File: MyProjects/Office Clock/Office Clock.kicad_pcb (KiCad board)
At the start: 2 copper layers, 105.4 x 97.8 mm, 13 parts, among them M1 DLX3416, M2 DLX3416, Q1 Q_Photo_NPN_CE, U1 MAX7219, U2 D1_Mini, U3 74HCT367N, U4 74HCT164N

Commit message: Finished schematic wiring
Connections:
- M1 pad 1: Net-(M1-Pad1) -> +5V
- M1 pad 10: Net-(M1-Pad10) -> +5V
- M1 pad 11: Net-(M1-Pad11) -> GND
- M1 pad 12: Net-(M1-Pad12) -> GND
- M1 pad 14: Net-(M1-Pad14) -> +5V
- M1 pad 16: Net-(M1-Pad16) -> /d0
- M1 pad 17: Net-(M1-Pad17) -> /d1
- M1 pad 18: Net-(M1-Pad18) -> /d2
- M1 pad 19: Net-(M1-Pad19) -> /d3
- M1 pad 2: Net-(M1-Pad2) -> +5V
- M1 pad 20: Net-(M1-Pad20) -> /d4
- M1 pad 21: Net-(M1-Pad21) -> /d5
- M1 pad 22: Net-(M1-Pad22) -> /d6
- M1 pad 4: Net-(M1-Pad4) -> GND
- M1 pad 5: Net-(M1-Pad5) -> +5V
- M1 pad 6: Net-(M1-Pad6) -> +5V
- M2 pad 1: Net-(M2-Pad1) -> /sel
- M2 pad 10: Net-(M2-Pad10) -> +5V
- M2 pad 11: Net-(M2-Pad11) -> GND
- M2 pad 12: Net-(M2-Pad12) -> GND
- M2 pad 14: Net-(M2-Pad14) -> +5V
- M2 pad 16: Net-(M2-Pad16) -> /d0
- M2 pad 17: Net-(M2-Pad17) -> /d1
- M2 pad 18: Net-(M2-Pad18) -> /d2
- M2 pad 19: Net-(M2-Pad19) -> /d3
- M2 pad 2: Net-(M2-Pad2) -> +5V
- M2 pad 20: Net-(M2-Pad20) -> /d4
- M2 pad 21: Net-(M2-Pad21) -> /d5
- M2 pad 22: Net-(M2-Pad22) -> /d6
- M2 pad 3: Net-(M2-Pad3) -> GND
- M2 pad 4: Net-(M2-Pad4) -> GND
- M2 pad 5: Net-(M2-Pad5) -> +5V
- M2 pad 6: Net-(M2-Pad6) -> +5V
- M2 pad 7: Net-(M2-Pad7) -> Net-(M1-Pad7)
- M2 pad 8: Net-(M2-Pad8) -> Net-(M1-Pad8)
- M2 pad 9: Net-(M2-Pad9) -> Net-(M1-Pad9)
- U2 pad 14: Net-(S1-Pad1) -> Net-(U2-Pad14)
- U2 pad 16: Net-(U2-Pad16) -> +3V3
- U3 pad 10: Net-(U3-Pad10) -> Net-(U2-Pad5)
- U3 pad 11: Net-(U3-Pad11) -> Net-(M1-Pad8)
- U3 pad 12: Net-(U3-Pad12) -> Net-(U2-Pad6)
- U3 pad 13: Net-(U3-Pad13) -> Net-(M1-Pad9)
- U3 pad 14: Net-(U3-Pad14) -> Net-(U2-Pad14)
- U3 pad 9: Net-(U3-Pad9) -> Net-(M1-Pad7)
- U4 pad 1: Net-(U4-Pad1) -> Net-(U2-Pad13)
- U4 pad 10: Net-(U4-Pad10) -> /d4
- U4 pad 11: Net-(U4-Pad11) -> /d5
- U4 pad 12: Net-(U4-Pad12) -> /d6
- U4 pad 13: Net-(U4-Pad13) -> /sel
- U4 pad 14: Net-(U4-Pad14) -> +5V
- U4 pad 2: Net-(U4-Pad2) -> Net-(U2-Pad13)
- U4 pad 3: Net-(U4-Pad3) -> /d0
- U4 pad 4: Net-(U4-Pad4) -> /d1
- U4 pad 5: Net-(U4-Pad5) -> /d2
- U4 pad 6: Net-(U4-Pad6) -> /d3
- U4 pad 7: Net-(U4-Pad7) -> GND
- U4 pad 8: Net-(U4-Pad8) -> Net-(U2-Pad3)

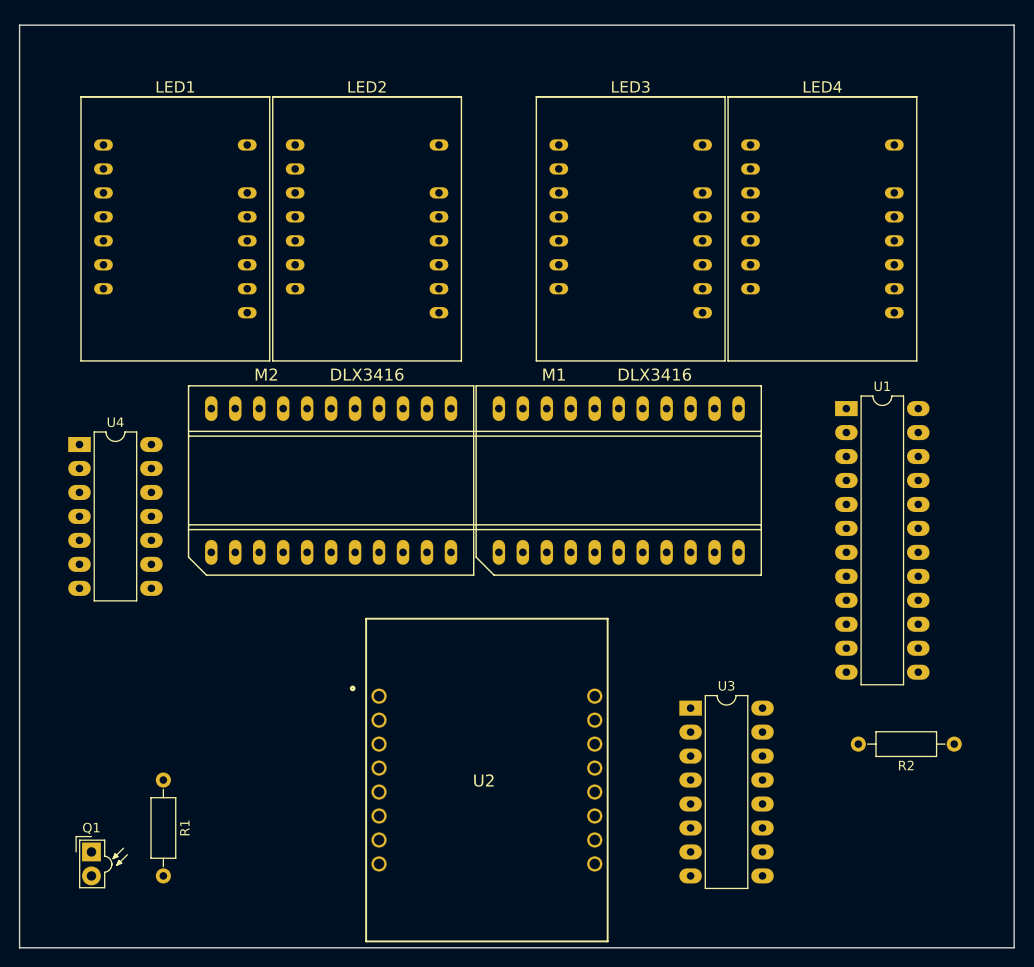
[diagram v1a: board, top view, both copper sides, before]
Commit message: Finished laying out board with filled zones
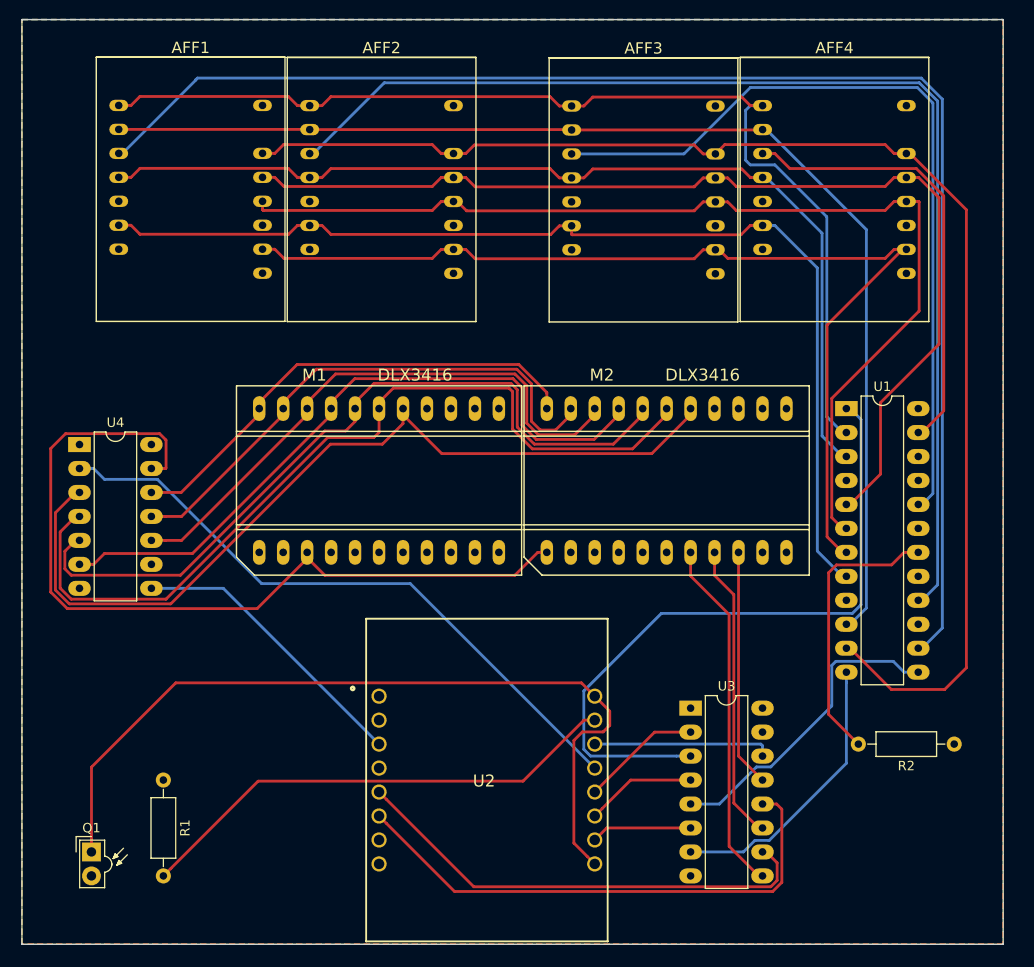
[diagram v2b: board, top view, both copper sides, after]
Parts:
- removed LED1, LED2, LED3, LED4: LN518GA, LN518xx:LN518xx
- added AFF1: LN518xx, LN518xx:LN518xx, F.Cu at (49.9, 39.0)
- added AFF2: LN518xx, LN518xx:LN518xx, F.Cu at (70.1, 39.0)
- added AFF3: LN518xx, LN518xx:LN518xx, F.Cu at (97.9, 39.0)
- added AFF4: LN518xx, LN518xx:LN518xx, F.Cu at (118.1, 39.0)
- moved M2 35.6 mm to (102.9, 69.8)
- moved M1 25.4 mm to (72.4, 69.8)
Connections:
- M1 pad 3: Net-(M1-Pad3) -> /sel
- U3 pad 2: Net-(U2-Pad10) -> Net-(U2-Pad12)
- U3 pad 6: Net-(U2-Pad12) -> Net-(U2-Pad10)
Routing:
- net Net-(AFF1-Pad3): track 0.00 -> 151.0 mm
- net /b: track 0.00 -> 143.4 mm
- net /f: track 0.00 -> 127.4 mm
- net Net-(AFF2-Pad3): track 0.00 -> 124.5 mm
- net /a: track 0.00 -> 113.3 mm
- net /ldp: track 0.00 -> 113.0 mm
- net /c: track 0.00 -> 111.8 mm
- net /g: track 0.00 -> 111.8 mm
- net /d: track 0.00 -> 107.5 mm
- net /e: track 0.00 -> 104.3 mm
- net /d0: track 0.00 -> 93.1 mm
- net /d1: track 0.00 -> 91.7 mm
- net /sel: track 0.00 -> 91.4 mm
- net +3V3: track 0.00 -> 88.8 mm
- net Net-(AFF3-Pad3): track 0.00 -> 85.3 mm
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- added copper zone on B.Cu, net (none)
- added copper zone on F.Cu, net (none)
- added copper zone on F.Cu, net +5V
- added copper zone on B.Cu, net GND
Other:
- board size 105.4 x 97.8 mm -> 104 x 98 mm
- net class Wider Track: clearance 0.5 -> 0.2

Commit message: Finished laying out 2 sided PCB with fill
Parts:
- added REF**: 1pin, Connectors:1pin, F.Cu at (131.0, 26.0)
- added REF**: 1pin, Connectors:1pin, F.Cu at (37.0, 26.0)
- added REF**: 1pin, Connectors:1pin, F.Cu at (37.0, 114.0)
- added REF**: 1pin, Connectors:1pin, F.Cu at (131.0, 114.0)
- moved Q1 6.43 mm to (41.0, 103.0)
- moved R1 3.00 mm to (47.0, 98.6)
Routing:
- net +5V: track 4.62 -> 258.3 mm
- net +3V3: track 88.8 -> 81.9 mm
- net Net-(Q1-Pad2): track 52.6 -> 58.6 mm
- net /sel: track 91.4 -> 93.6 mm
- added copper zone on F.Cu, net GND
- removed copper zone on B.Cu, net (none)
- removed copper zone on F.Cu, net (none)
- removed copper zone on F.Cu, net +5V
